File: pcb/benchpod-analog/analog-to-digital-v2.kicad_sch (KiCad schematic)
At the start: 50 parts, among them J8 Screw_Terminal_01x02, K3 G6K-2F-Y DC5, K4 G6K-2F-Y DC5, U11 HX PZ2.54-1X2P ZZ, U17 TMCP1A106MTRF, U36 MCP33131D-10-E/MS, U37 THS4551IRUNR, U40 OPA810IDBVR

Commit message: analog only board: enclosure connectors (BNC, pluggable 4-20 mA blocks)
Per benchpod-private enclosure/design.md:
- RF2 (0-5 V), RF3 (+-12 V), RF4 (ADC in): SMA -> right-angle BNC
  KH-BNC50-3511 (C2837587). Center on the same net, shell + lugs to GND.
- RF1 (0-3.3 V jack) removed; the 0-3.3 V output stays on TP1.
- 2-pin test headers U11-U14 and their 0 ohm links R20, R165-R167 removed;
  test pads TP1-TP4 (1.5 mm, not in the BOM) on the four outputs instead.
- J8 (4-20 mA in) and J9 (4-20 mA out): 5.08 mm screw terminals ->
  3.81 mm right-angle pluggable WJ15EDGRC-3.81-02P (C8387, green); the
  mating plug C8466 is bought separately.

Co-Authored-By: Claude Opus 5.5 <noreply@anthropic.com>
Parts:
- removed R20: 0, Resistor_SMD:R_0402_1005Metric, symbol Device:R
- removed RF4: HC-SMA-KWE-14.5H-D002-01, lcsc:SMA-TH_BWSMA-KWE-Z001, symbol lcsc_lib:BWSMA-KWE-Z001
- removed U11: HX PZ2.54-1X2P ZZ, lcsc_footprints:C32713268_HDR-TH_2P-P2_54-V-M-3, symbol lcsc_plugin:HX_PZ2_54-1X2P_ZZ
- added RF4: KH-BNC50-3511, lcsc_footprints:C2837587_ANT-TH_KH-BNC50-3511, symbol lcsc_imported:KH-BNC50-3511_C2837587
- added TP4: TP ADC in, TestPoint:TestPoint_Pad_D1.5mm, symbol Connector:TestPoint
- J8: value Screw_Terminal_01x02 -> WJ15EDGRC-3.81-02P; footprint lcsc:CONN-TH_2P-P5.00_WJ500V-5.08-2P -> lcsc_footprints:C8387_CONN-TH_2P-P3.81_WJ15EDGRC-3.81-2P; LCSC C8465 -> C8387
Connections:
- net GND: now also RF4.2 (GND), RF4.3 (MNT), RF4.4 (MNT)
- net RELAY1_IN: now also RF4.1 (OUT), TP4.1

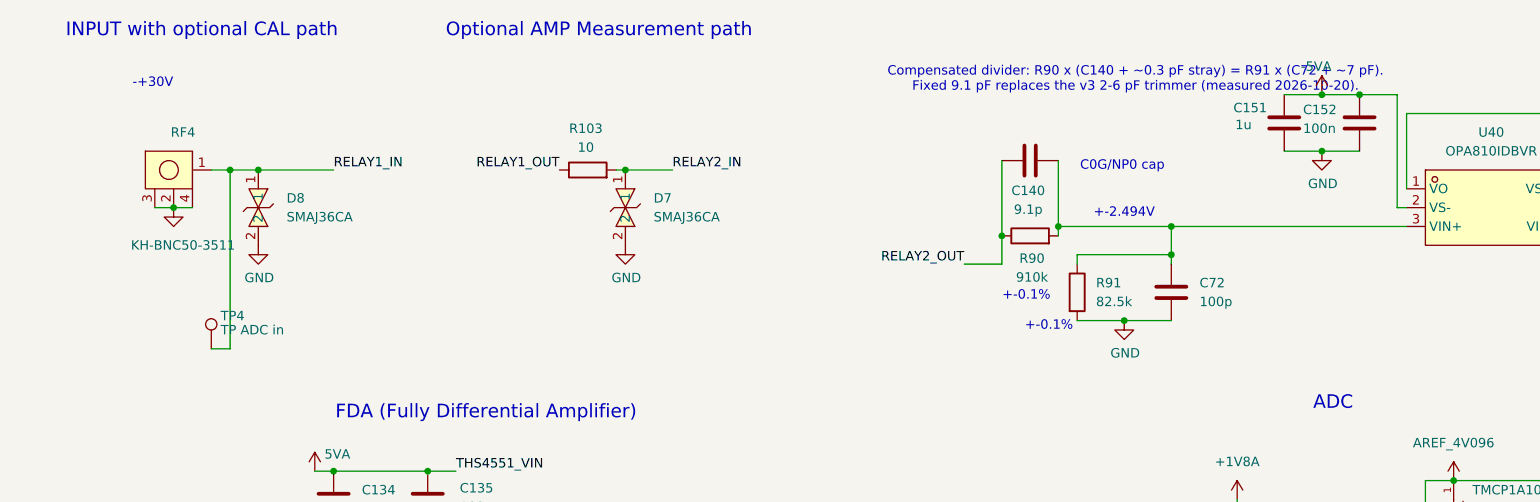
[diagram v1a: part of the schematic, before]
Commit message: analog only board: ADC input ready for 10x probes, lead-free BNC
- J10 (was RF4): ADC input BNC is now the lead-free SAMZO BNC-KYWE-295-W4-N
  (C41416668), as decided in benchpod-compliance v4-parts.md; the Kinghelm
  KH-BNC50-3511 relies on a RoHS lead exemption and is removed (symbol,
  footprint, model).
- D8 and D7 (SMAJ36CA on RELAY1_IN / RELAY2_IN) removed: a few hundred pF and
  uA leakage on the 1 Mohm node made 10x probes impossible to compensate.
- D22 BAV199LT1G (C145516, pA leakage, ~2 pF) clamps the OPA810 input
  (R90/R91 node) to 5VA / -5VA. R90 limits the fault current (0.33 mA at
  300 V) and moves to a 1206 0.1 % 200 V part (YAGEO RT1206BRD07910KL,
  C870935), value unchanged (910k + 82.5k = 992.5 kohm, ratio unchanged).
- Result: about 1 Mohm || 15-20 pF at the BNC, so 1x leads and normal 10x
  probes both work; 10x needs a 1x/10x setting with its own gain cal in
  firmware. D22 adds ~2 pF on the R91 side: check the divider compensation
  (C140) on the first board. D6 (4-20 mA input) keeps its SMAJ36CA.

Co-Authored-By: Claude Opus 5.5 <noreply@anthropic.com>
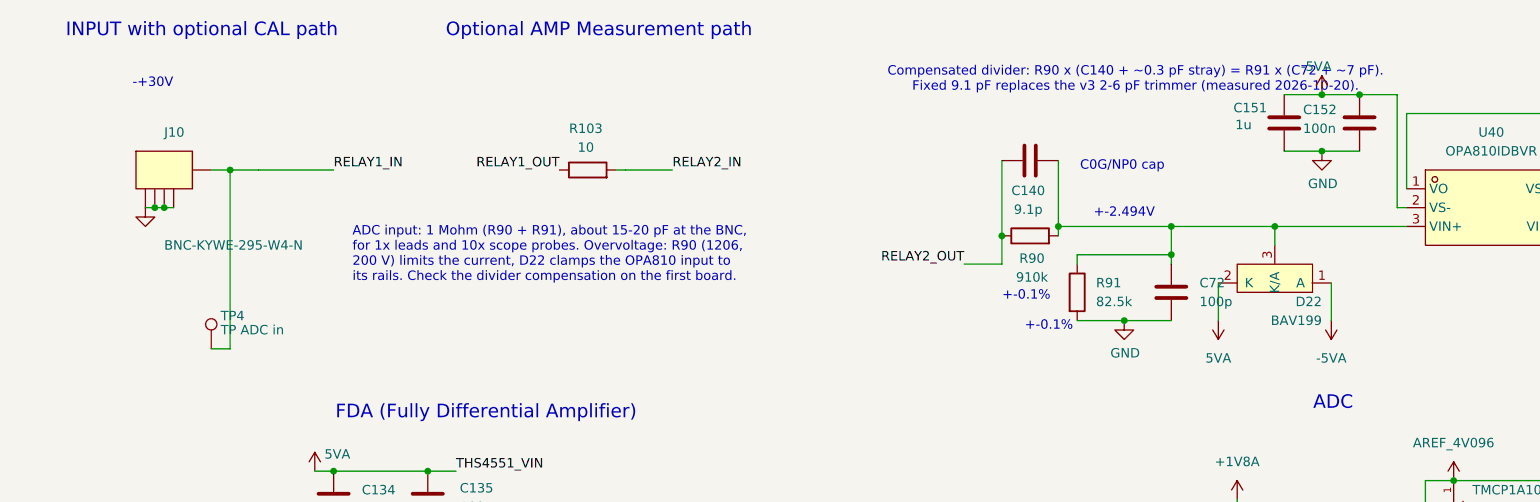
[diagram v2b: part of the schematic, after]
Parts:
- removed D7, D8: SMAJ36CA, lcsc:SMA_L4.3-W2.6-LS5.0-BI, symbol lcsc_lib:SMAJ36CA_C19077551
- removed RF4: KH-BNC50-3511, lcsc_footprints:C2837587_ANT-TH_KH-BNC50-3511, symbol lcsc_imported:KH-BNC50-3511_C2837587
- added D22: BAV199, lcsc_footprints:C145516_SOT-23_L2.9-W1.3-P1.90-LS2.4-BR, symbol lcsc_imported:BAV199LT1G_C145516
- added J10: BNC-KYWE-295-W4-N, lcsc_footprints:C41416668_BNC-TH_BNC-KYWE-295-W4-N, symbol lcsc_imported:BNC-KYWE-295-W4-N_C41416668
- R90: footprint Resistor_SMD:R_0603_1608Metric -> Resistor_SMD:R_1206_3216Metric; LCSC C2686431 -> C870935
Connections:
- net -5VA: now also D22.1 (A)
- net 5VA: now also D22.2 (K)
- net GND: now also J10.1 (GND), J10.2 (GND), J10.3 (GND), J10.4 (GND)
- net RELAY1_IN: now also J10.5 (OUT)
- net at C140.2, C72.1, R90.2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: now also D22.3 (K/A)
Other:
- note added: "ADC input: 1 Mohm (R90 + R91), about 15-20 pF at the BNC, for 1x leads and 10x scope probes. Overvoltage: R90 (1206, 200 V) limits the current, D22 clamps the OPA810 input to its rails. Check the divider compensation on the first board."
